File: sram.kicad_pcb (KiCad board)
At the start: 4 copper layers, 25 parts, among them J1 Cache_slot, M1 UM61256AS, M2 UM61256AS, M3 UM61256AS, M4 UM61256AS, M5 UM61256AS, M6 UM61256AS, M7 UM61256AS, M8 UM61256AS, U1 74HCT244, U2 74HCT244

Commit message: 3 errors, 76 warnings
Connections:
- net M1_WE# renamed WE_byte0
- net M8_WE# renamed WE_8
- net Net-(J1-PadA19) renamed under_U1_3
- net Net-(J1-PadA25) renamed under_U1_2
- net U1_2A0 renamed CPU_A8
- net U1_2A1 renamed CPU_A7
- net U1_2A2 renamed CPU_A6
- net U1_2A3 renamed CPU_A5
- net U2_2A0 renamed CPU_A17
- net U2_2A1 renamed CPU_A15
- net U2_2A3 renamed CPU_A16
- net a10 renamed under_tag6
- net a11 renamed under_tag7
- net a13 renamed under_tag8
- net a15 renamed under_tag9
- net a17 renamed under_tag10
- net a18 renamed under_tag11
- net a2 renamed under_tag12
- net a3 renamed under_tag13
- net a35 renamed under_U1_1
- net a4 renamed under_tag14
- net a51 renamed CPU_A13
- net a8 renamed under_tag5
- J1 pad A1: a1 -> unconnected-(J1-PadA1)
- J1 pad A30: a30 -> unconnected-(J1-PadA30)
- J1 pad A31: a31 -> unconnected-(J1-PadA31)
- J1 pad A33: a33 -> unconnected-(J1-PadA33)
- J1 pad A34: a34 -> unconnected-(J1-PadA34)
- J1 pad A42: a42 -> CPU_A9
- J1 pad A43: a43 -> CPU_A10
- J1 pad A45: a45 -> CPU_A11
- J1 pad A46: a46 -> CPU_A12
- J1 pad A49: U2_2A2 -> CPU_A14
- J1 pad A54: a54 -> unconnected-(J1-PadA54)
- J1 pad A55: a55 -> unconnected-(J1-PadA55)
- J1 pad A6: a6 -> unconnected-(J1-PadA6)
- J1 pad A7: a7 -> unconnected-(J1-PadA7)
- J1 pad B15: b15 -> CPU_D31
- J1 pad B16: b16 -> CPU_D30
- J1 pad B17: b17 -> CPU_D29
- J1 pad B19: b19 -> CPU_D28
- J1 pad B20: b20 -> CPU_D27
- J1 pad B21: b21 -> CPU_D26
- J1 pad B23: b23 -> CPU_D25
- J1 pad B24: b24 -> CPU_D24
- J1 pad B25: b25 -> CPU_D23
- J1 pad B27: b27 -> CPU_D22
- J1 pad B28: b28 -> CPU_D21
- J1 pad B29: b29 -> CPU_D20
- J1 pad B31: b31 -> CPU_D19
- J1 pad B32: M3_Q2 -> CPU_D18
- J1 pad B33: M3_Q1 -> CPU_D17
- J1 pad B35: M3_Q0 -> CPU_D16
- J1 pad B36: M6_Q7 -> CPU_D15
- J1 pad B37: M6_Q6 -> CPU_D14
- J1 pad B39: b39 -> CPU_D13
- J1 pad B40: b40 -> CPU_D12
- J1 pad B41: b41 -> CPU_D11
- J1 pad B43: M6_Q2 -> CPU_D10
- J1 pad B44: M6_Q1 -> CPU_D9
- J1 pad B45: M6_Q0 -> CPU_D8
- J1 pad B47: M5_Q7 -> CPU_D7
- J1 pad B48: M5_Q6 -> CPU_D6
- J1 pad B49: M5_Q5 -> CPU_D5
- J1 pad B51: M5_Q4 -> CPU_D4
- J1 pad B52: M5_Q3 -> CPU_D3
- J1 pad B53: M5_Q2 -> CPU_D2
- J1 pad B55: M5_Q1 -> CPU_D1
- J1 pad B56: M5_Q0 -> CPU_D0
- M1 pad 11: M1_Q0 -> CPU_D0
- M1 pad 12: M1_Q1 -> CPU_D1
- M1 pad 13: M1_Q2 -> CPU_D2
- M1 pad 15: M1_Q3 -> CPU_D3
- M1 pad 16: M1_Q4 -> CPU_D4
- M1 pad 17: M1_Q5 -> CPU_D5
- M1 pad 18: M1_Q6 -> CPU_D6
- M1 pad 19: M1_Q7 -> CPU_D7
- M1 pad 20: unconnected-(M1-~{CS}-Pad20) -> Bank0_CS
- M1 pad 22: unconnected-(M1-~{OE}-Pad22) -> Bank0_OE
- M2 pad 11: M2_Q0 -> CPU_D8
- M2 pad 12: M2_Q1 -> CPU_D9
- M2 pad 13: M2_Q2 -> CPU_D10
- M2 pad 15: M2_Q3 -> CPU_D11
- M2 pad 16: M2_Q4 -> CPU_D12
- M2 pad 17: M2_Q5 -> CPU_D13
- M2 pad 18: M2_Q6 -> CPU_D14
- M2 pad 19: M2_Q7 -> CPU_D15
- M2 pad 20: unconnected-(M2-~{CS}-Pad20) -> Bank0_CS
- M2 pad 22: unconnected-(M2-~{OE}-Pad22) -> Bank0_OE
- M3 pad 11: M3_Q0 -> CPU_D16
- M3 pad 12: M3_Q1 -> CPU_D17
- M3 pad 13: M3_Q2 -> CPU_D18
- M3 pad 15: M3_Q3 -> CPU_D19
- M3 pad 16: M3_Q4 -> CPU_D20
- M3 pad 17: M3_Q5 -> CPU_D21
- M3 pad 18: M3_Q6 -> CPU_D22
- M3 pad 19: M3_Q7 -> CPU_D23
- M3 pad 20: unconnected-(M3-~{CS}-Pad20) -> Bank0_CS
- M3 pad 22: unconnected-(M3-~{OE}-Pad22) -> Bank0_OE
- M4 pad 11: M4_Q0 -> CPU_D24
- M4 pad 12: M4_Q1 -> CPU_D25
- M4 pad 13: M4_Q2 -> CPU_D26
- M4 pad 15: M4_Q3 -> CPU_D27
- M4 pad 16: M4_Q4 -> CPU_D28
- M4 pad 17: M4_Q5 -> CPU_D29
- M4 pad 18: M4_Q6 -> CPU_D30
- M4 pad 19: M4_Q7 -> CPU_D31
- M4 pad 20: unconnected-(M4-~{CS}-Pad20) -> Bank0_CS
- M4 pad 22: unconnected-(M4-~{OE}-Pad22) -> Bank0_OE
- M5 pad 11: M5_Q0 -> CPU_D0
- M5 pad 12: M5_Q1 -> CPU_D1
- M5 pad 13: M5_Q2 -> CPU_D2
- M5 pad 15: M5_Q3 -> CPU_D3
- M5 pad 16: M5_Q4 -> CPU_D4
- M5 pad 17: M5_Q5 -> CPU_D5
- M5 pad 18: M5_Q6 -> CPU_D6
- M5 pad 19: M5_Q7 -> CPU_D7
- M5 pad 20: unconnected-(M5-~{CS}-Pad20) -> Bank1_CS
- M5 pad 22: unconnected-(M5-~{OE}-Pad22) -> Bank1_OE
- M6 pad 11: M6_Q0 -> CPU_D8
- M6 pad 12: M6_Q1 -> CPU_D9
- M6 pad 13: M6_Q2 -> CPU_D10
- M6 pad 15: M6_Q3 -> CPU_D11
- M6 pad 16: M6_Q4 -> CPU_D12
- M6 pad 17: M6_Q5 -> CPU_D13
- M6 pad 18: M6_Q6 -> CPU_D14
- M6 pad 19: M6_Q7 -> CPU_D15
- M6 pad 20: unconnected-(M6-~{CS}-Pad20) -> Bank1_CS
- M6 pad 22: unconnected-(M6-~{OE}-Pad22) -> Bank1_OE
- M7 pad 11: M7_Q0 -> CPU_D16
- M7 pad 12: M7_Q1 -> CPU_D17
- M7 pad 13: M7_Q2 -> CPU_D18
- M7 pad 15: M7_Q3 -> CPU_D19
- M7 pad 16: M7_Q4 -> CPU_D20
- M7 pad 17: M7_Q5 -> CPU_D21
- M7 pad 18: M7_Q6 -> CPU_D22
- M7 pad 19: M7_Q7 -> CPU_D23
- M7 pad 20: unconnected-(M7-~{CS}-Pad20) -> Bank1_CS
- M7 pad 22: unconnected-(M7-~{OE}-Pad22) -> Bank1_OE
- M7 pad 27: unconnected-(M7-~{WE}-Pad27) -> WE_7
- M8 pad 11: M8_Q0 -> CPU_D24
- M8 pad 12: M8_Q1 -> CPU_D25
- M8 pad 13: M8_Q2 -> CPU_D26
- M8 pad 15: M8_Q3 -> CPU_D27
- M8 pad 16: M8_Q4 -> CPU_D28
- M8 pad 17: M8_Q5 -> CPU_D29
- M8 pad 18: M8_Q6 -> CPU_D30
- M8 pad 19: M8_Q7 -> CPU_D31
- M8 pad 20: unconnected-(M8-~{CS}-Pad20) -> Bank1_CS
- M8 pad 22: unconnected-(M8-~{OE}-Pad22) -> Bank1_OE
- MD1 pad 21: MD1_A10 -> CPU_A14
- MD1 pad 24: MD1_A9 -> CPU_A12
- MD1 pad 25: MD1_A8 -> CPU_A11
- R6 pad 1: unconnected-(R6-Pad1) -> under_tag3
- U1 pad 6: unconnected-(U1-1A2-Pad6) -> under_tag4
- U2 pad 12: unconnected-(U2-1Y3-Pad12) -> CPU_A4_SR
- U2 pad 13: U2_2A2 -> CPU_A14
- U2 pad 2: unconnected-(U2-1A0-Pad2) -> CPU_A12
- U2 pad 4: MD1_A8 -> CPU_A11
- U2 pad 6: unconnected-(U2-1A2-Pad6) -> CPU_A10
- U2 pad 8: unconnected-(U2-1A3-Pad8) -> CPU_A9
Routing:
- net Bank1_OE: track 0.00 -> 163.9 mm, vias 0 -> 8
- net (no net): track 312.1 -> 155.4 mm, vias 32 -> 8
- net Bank0_OE: track 0.00 -> 151.3 mm, vias 0 -> 4
- net Bank0_CS: track 0.00 -> 120.9 mm, vias 0 -> 3
- net Bank1_CS: track 0.00 -> 113.4 mm, vias 0 -> 2
- net unconnected-(M4-~{CS}-Pad20): track 92.0 -> 0.00 mm, vias 3 -> 0
- net unconnected-(M1-~{OE}-Pad22): track 88.8 -> 0.00 mm, vias 2 -> 0
- net unconnected-(M5-~{OE}-Pad22): track 86.5 -> 0.00 mm, vias 3 -> 0
- net unconnected-(M5-~{CS}-Pad20): track 81.9 -> 0.00 mm, vias 2 -> 0
- net CPU_A14: track 0.00 -> 56.9 mm, vias 0 -> 2
- net CPU_A12: track 0.00 -> 55.1 mm, vias 0 -> 2
- net CPU_A11: track 0.00 -> 52.2 mm, vias 0 -> 2
- net CPU_A9: track 0.00 -> 51.6 mm
- net CPU_A4_SR: track 78.8 -> 128.9 mm, vias 4 -> 6
- net CPU_A10: track 0.00 -> 48.7 mm
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
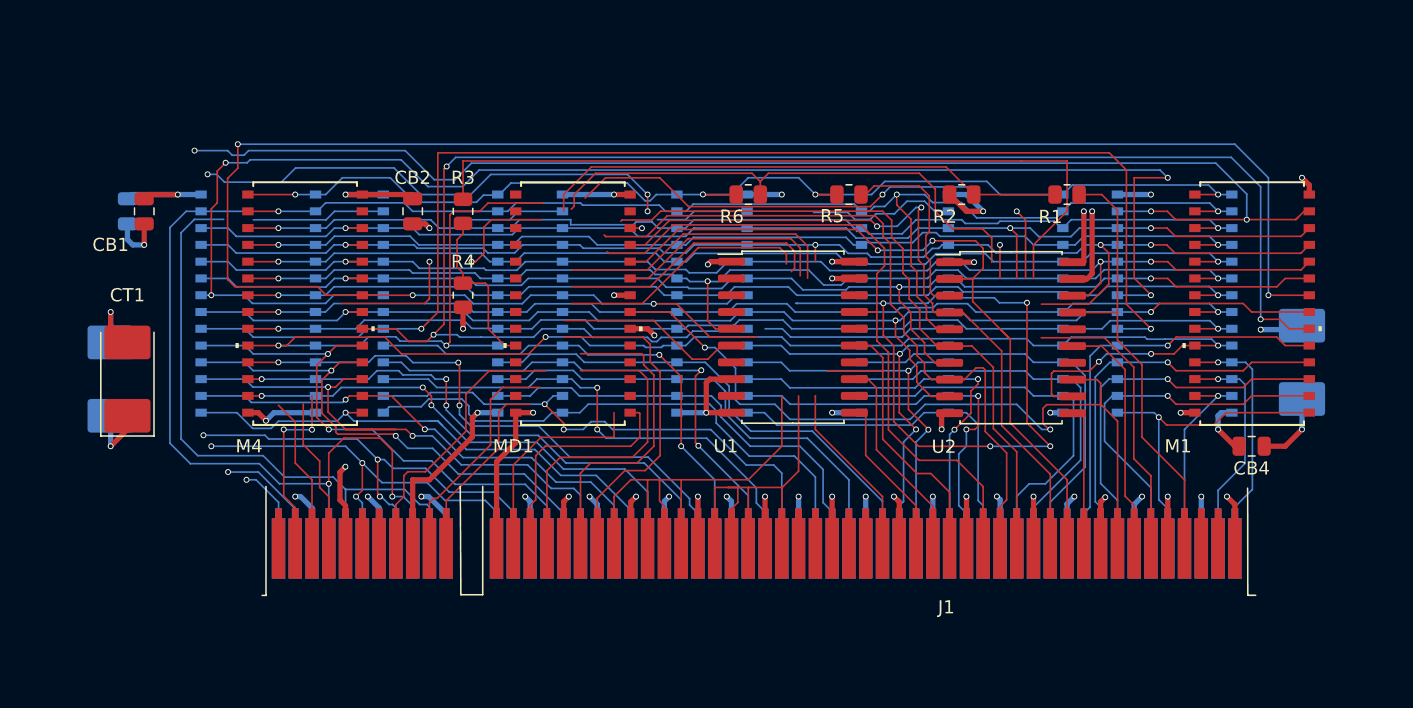
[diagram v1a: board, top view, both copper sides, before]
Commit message: 0 drc errors, 62 violations
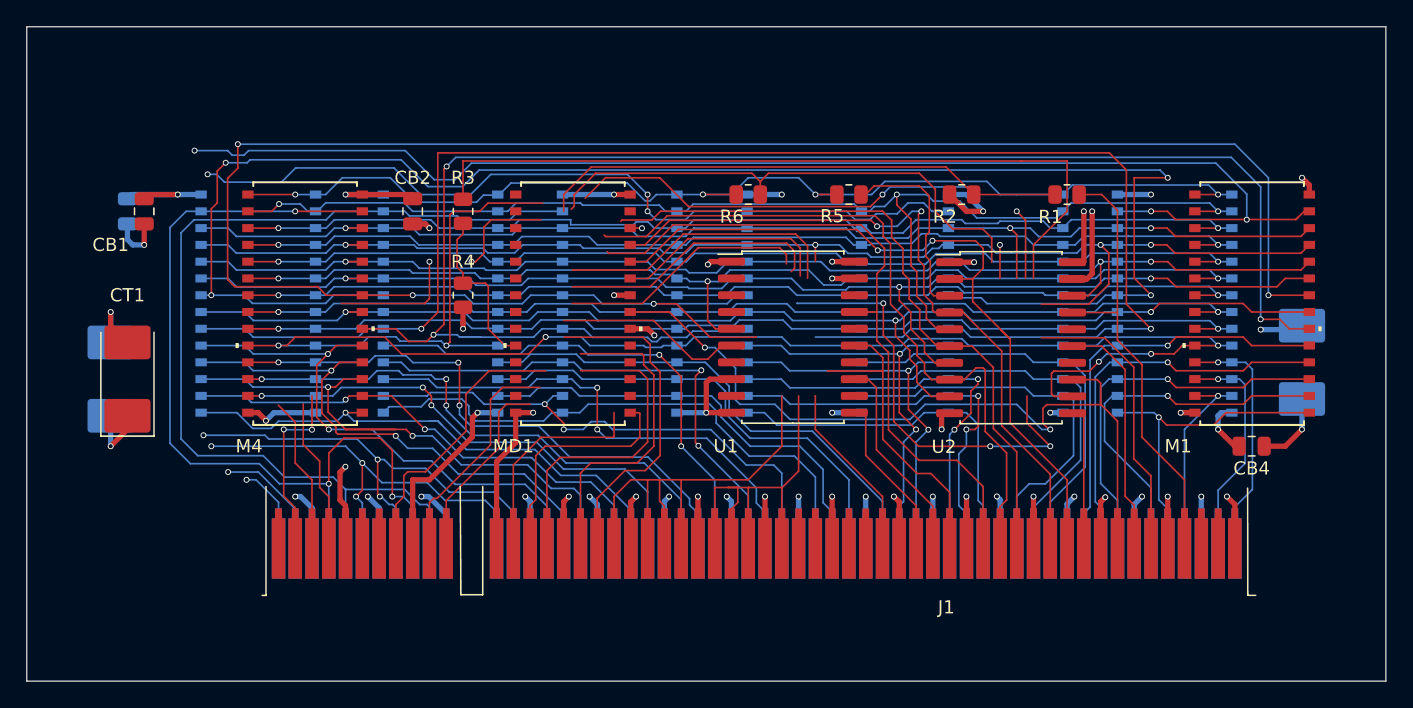
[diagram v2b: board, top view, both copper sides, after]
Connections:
- net ?1 renamed under_sticker1
- net ?2 renamed under_sticker2
- net ?3 renamed under_sticker3
- net ?4 renamed under_sticker4
- J1 pad B10: ?7 -> WE_byte2
- J1 pad B4: WE_8 -> WE_byte3
- J1 pad B5: ?7 -> WE_byte2
- J1 pad B9: WE_8 -> WE_byte3
- M2 pad 27: unconnected-(M2-~{WE}-Pad27) -> WE_byte1
- M3 pad 27: unconnected-(M3-~{WE}-Pad27) -> WE_byte2
- M4 pad 27: unconnected-(M4-~{WE}-Pad27) -> WE_byte3
- M6 pad 27: unconnected-(M6-~{WE}-Pad27) -> WE_byte1
- M7 pad 27: WE_7 -> WE_byte2
- M8 pad 27: WE_8 -> WE_byte3
- R3 pad 2: unconnected-(R3-Pad2) -> under_U2_4
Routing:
- net WE_byte2: track 0.00 -> 69.0 mm
- net WE_byte1: track 0.00 -> 61.7 mm, vias 0 -> 3
- net WE_byte3: track 0.00 -> 60.8 mm, vias 0 -> 3
- net under_U2_4: track 0.00 -> 58.6 mm
- net unconnected-(R3-Pad2): track 58.6 -> 0.00 mm
- net WE_8: track 51.9 -> 0.00 mm, vias 2 -> 0
- net ?7: track 42.5 -> 0.00 mm
- net Bank1_OE: track 163.9 -> 125.6 mm, vias 8 -> 4
- net unconnected-(M6-~{WE}-Pad27): track 11.3 -> 0.00 mm
- net WE_7: track 10.1 -> 0.00 mm
- net Bank1_CS: track 113.4 -> 122.7 mm
- net unconnected-(M3-~{WE}-Pad27): track 7.92 -> 0.00 mm
- net unconnected-(M2-~{WE}-Pad27): track 7.04 -> 0.00 mm
- net (no net): track 155.4 -> 150.9 mm
- net Bank0_CS: track 120.9 -> 122.5 mm
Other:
- board outline added: 102.9 x 49.5 mm

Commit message: 90% there, 0 errors 18 warnings. Just a couple tracks left.
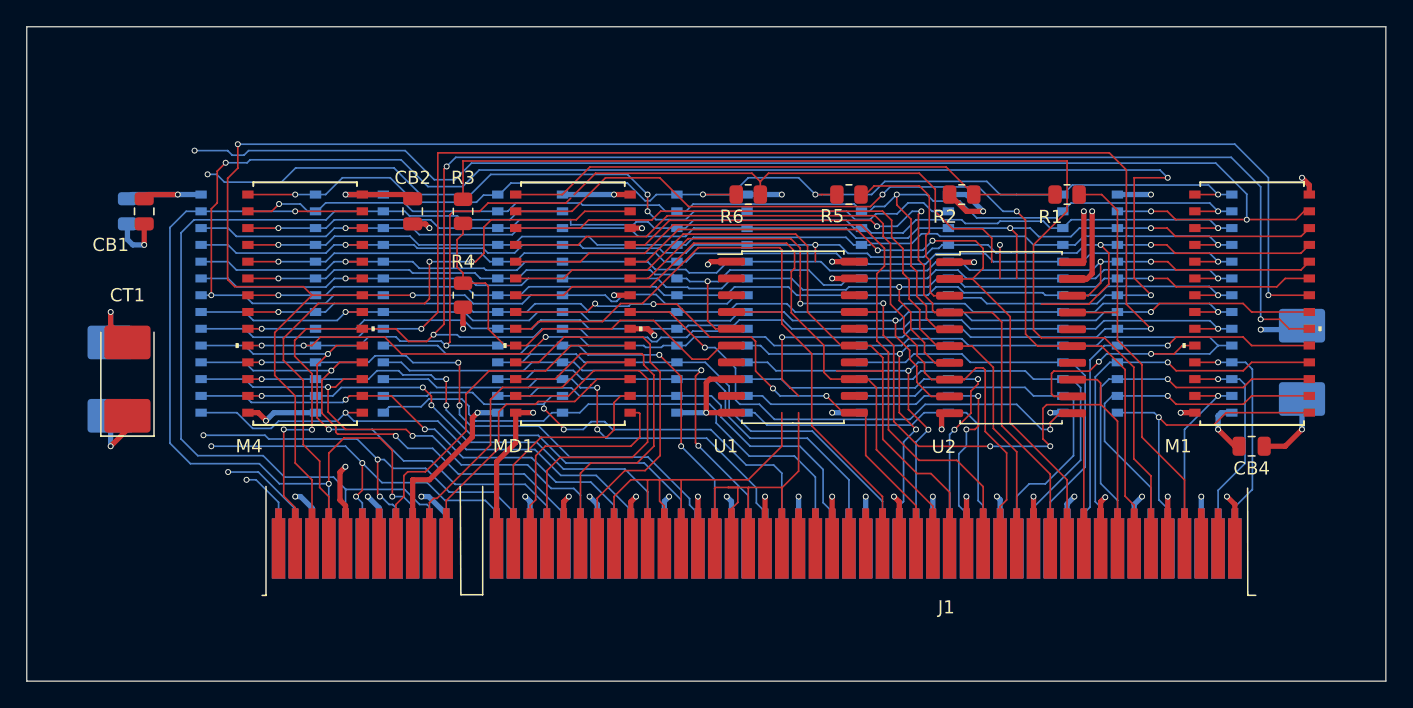
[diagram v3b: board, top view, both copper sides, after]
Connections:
- net WE_byte0 renamed Byte_WE0
- net WE_byte1 renamed Byte_WE1
- net WE_byte2 renamed Byte_WE2
- net WE_byte3 renamed Byte_WE3
- J1 pad A10: under_tag6 -> TAG_Q6
- J1 pad A11: under_tag7 -> TAG_Q5
- J1 pad A13: under_tag8 -> TAG_Q4
- J1 pad A15: under_tag9 -> TAG_Q2
- J1 pad A17: under_tag10 -> TAG_Q1
- J1 pad A18: under_tag11 -> TAG_Q0
- J1 pad A2: under_tag12 -> Bank0_CS
- J1 pad A3: under_tag13 -> Bank0_OE
- J1 pad A4: under_tag14 -> TAG_WE
- J1 pad A8: under_tag5 -> TAG_Q7
- J1 pad B14: GND -> +5V
- J1 pad B18: GND -> +5V
- J1 pad B26: GND -> +5V
- J1 pad B38: GND -> +5V
- J1 pad B42: GND -> +5V
- J1 pad B46: GND -> +5V
- J1 pad B50: GND -> +5V
- J1 pad B7: GND -> +5V
- MD1 pad 1: MD1_A14 -> TAG_A14
- MD1 pad 10: MD1_A0 -> TAG_A0
- MD1 pad 2: MD1_A12 -> CPU_A15
- MD1 pad 21: CPU_A14 -> CPU_A16
- MD1 pad 23: MD1_A11 -> CPU_A14
- MD1 pad 26: MD1_A13 -> +5V
- MD1 pad 27: unconnected-(MD1-~{WE}-Pad27) -> TAG_WE
- MD1 pad 3: MD1_A7 -> CPU_A10
- MD1 pad 4: MD1_A6 -> CPU_A9
- MD1 pad 5: MD1_A5 -> CPU_A8
- MD1 pad 6: MD1_A4 -> CPU_A7
- MD1 pad 7: MD1_A3 -> CPU_A6
- MD1 pad 8: MD1_A2 -> CPU_A5
- MD1 pad 9: MD1_A1 -> under_U1_1
- R1 pad 1: Net-(R1-Pad1) -> TAG_A14
- R2 pad 2: Net-(R1-Pad1) -> TAG_A14
- R3 pad 1: MD1_A0 -> TAG_A0
- R3 pad 2: under_U2_4 -> CPU_A13
- R4 pad 1: MD1_A0 -> TAG_A0
- R4 pad 2: GND -> +5V
- U1 pad 4: unconnected-(U1-1A1-Pad4) -> under_U1_1
- U1 pad 6: under_tag4 -> TAG_A0
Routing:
- net (no net): track 150.9 -> 2.54 mm, vias 8 -> 1
- net CPU_A13: track 19.5 -> 82.8 mm
- net under_U2_4: track 58.6 -> 0.00 mm
- net CPU_A15: track 15.9 -> 70.6 mm, vias 0 -> 2
- net TAG_WE: track 0.00 -> 47.7 mm, vias 0 -> 2
- net TAG_A14: track 0.00 -> 42.5 mm
- net CPU_A16: track 8.26 -> 48.7 mm, vias 0 -> 2
- net Net-(R1-Pad1): track 40.2 -> 0.00 mm
- net under_U1_1: track 11.0 -> 49.7 mm
- net CPU_A6: track 13.2 -> 49.0 mm
- net CPU_A7: track 21.2 -> 54.0 mm
- net TAG_A0: track 0.00 -> 31.5 mm
- net CPU_A5: track 10.1 -> 41.0 mm, vias 0 -> 4
- net TAG_Q2: track 0.00 -> 27.6 mm
- net TAG_Q0: track 0.00 -> 27.2 mm
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
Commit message: 95% there, 0 errors, 7 Warnings. 5 connections missing, 11 guesses and assumptions on U1 U2 and some more on common lines.
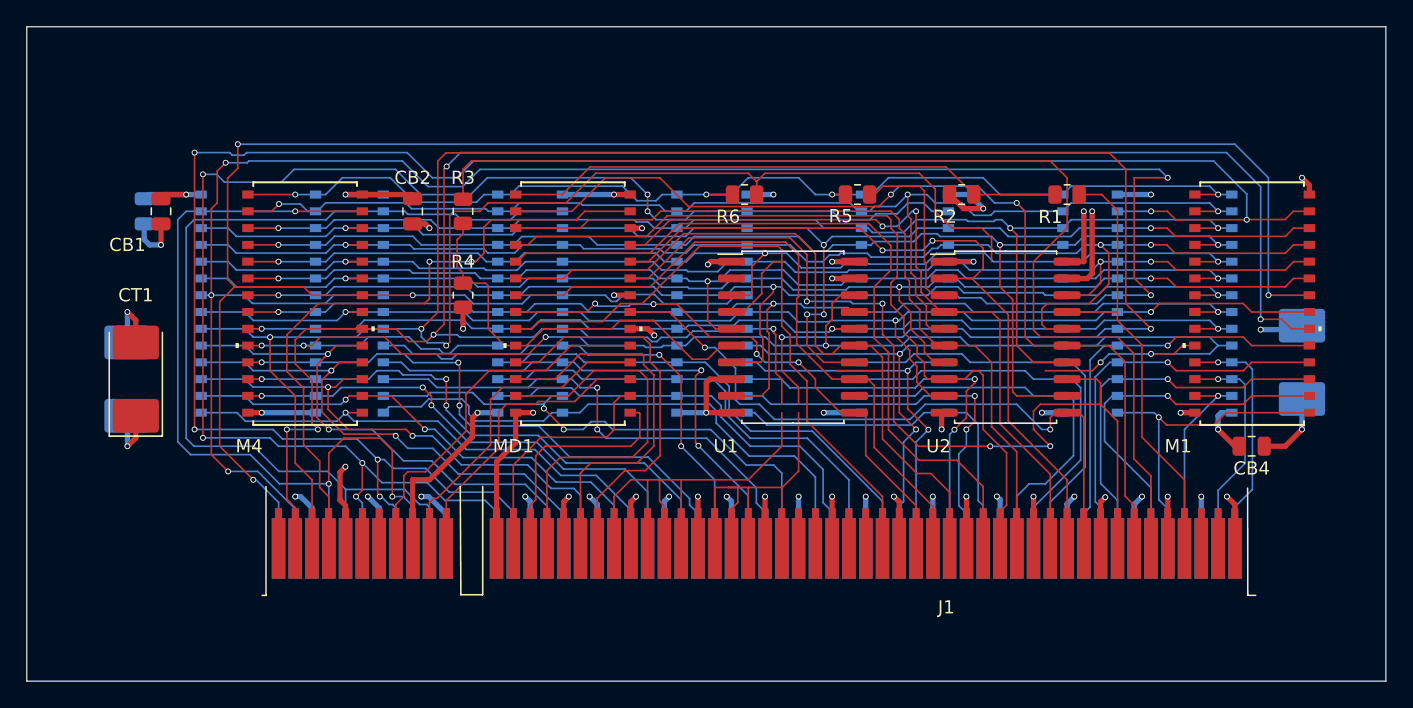
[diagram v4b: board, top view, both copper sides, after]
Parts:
- moved CB1 1.27 mm to (125.7, 83.8)
- moved CB3 1.27 mm to (124.5, 83.8)
- moved CT2 1.27 mm to (123.2, 96.5)
- moved R5 0.65 mm to (178.4, 82.5)
- moved CT1 0.64 mm to (123.8, 96.5)
- moved U2 0.41 mm to (189.7, 93.3)
- moved R6 0.28 mm to (169.9, 82.5)
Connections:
- net under_U1_1 renamed CPU_A4
- J1 pad A3: Bank0_OE -> Bank1_CS
- J1 pad A47: CPU_A16 -> CPU_A13
- J1 pad A51: CPU_A13 -> CPU_A16
- J1 pad B1: under_sticker3 -> Bank0_OE
- J1 pad B12: under_sticker1 -> Byte_WE1
- J1 pad B13: under_sticker2 -> Byte_WE0
- J1 pad B2: under_sticker4 -> Bank1_OE
- J1 pad B6: under_sticker1 -> Byte_WE1
- J1 pad B8: under_sticker2 -> Byte_WE0
- MD1 pad 21: CPU_A16 -> CPU_A13
- R3 pad 2: CPU_A13 -> CPU_A16
- R6 pad 1: under_tag3 -> Bank1_CS
- U1 pad 14: unconnected-(U1-1Y2-Pad14) -> CPU_A17_SR
- U1 pad 16: unconnected-(U1-1Y1-Pad16) -> CPU_A5_SR
- U1 pad 18: unconnected-(U1-1Y0-Pad18) -> CPU_A4_SR
- U1 pad 3: unconnected-(U1-2Y0-Pad3) -> CPU_A9_SR
- U1 pad 7: unconnected-(U1-2Y2-Pad7) -> CPU_A7_SR
- U1 pad 9: unconnected-(U1-2Y3-Pad9) -> CPU_A6_SR
- U2 pad 11: CPU_A16 -> CPU_A13
- U2 pad 12: CPU_A4_SR -> CPU_A10_SR
- U2 pad 14: unconnected-(U2-1Y2-Pad14) -> CPU_A11_SR
- U2 pad 16: unconnected-(U2-1Y1-Pad16) -> CPU_A12_SR
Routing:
- net Bank1_CS: track 130.1 -> 206.5 mm, vias 3 -> 5
- net Byte_WE0: track 99.3 -> 151.8 mm, vias 3 -> 6
- net Byte_WE1: track 61.7 -> 110.6 mm, vias 3 -> 6
- net under_tag3: track 38.6 -> 0.00 mm
- net CPU_A13: track 82.8 -> 48.9 mm, vias 0 -> 2
- net CPU_A16: track 48.7 -> 82.3 mm, vias 2 -> 0
- net under_sticker2: track 30.8 -> 0.00 mm, vias 3 -> 0
- net under_sticker1: track 28.0 -> 0.00 mm, vias 3 -> 0
- net Bank1_OE: track 125.6 -> 146.0 mm, vias 4 -> 5
- net CPU_A4_SR: track 132.9 -> 116.3 mm
- net CPU_A10_SR: track 79.0 -> 95.2 mm, vias 2 -> 3
- net CPU_A11_SR: track 79.7 -> 92.7 mm, vias 2 -> 3
- net CPU_A6_SR: track 78.8 -> 88.6 mm, vias 2 -> 3
- net CPU_A17_SR: track 92.3 -> 101.7 mm, vias 3 -> 5
- net Bank0_CS: track 142.5 -> 151.1 mm, vias 5 -> 6
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
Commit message: 99% done, ERC DRC 0 errors 0 warnings
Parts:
- CB1, CB2, CB3, CB4: value C -> 1uF 16V
- CT1, CT2, CT3: value C_Polarized -> 10uF 16V
- J1: footprint UM61256AS:Cache slot -> footprints:Cache slot
- M1, M2, M3, M4, M5, M6, M7, M8, MD1: footprint UM61256AS:SOJ28_18P54X7P75_ISI -> footprints:SOJ28_18P54X7P75_ISI
- U1, U2: value 74HCT244 -> 74F244
- moved J1 2.26 mm to (171.4, 109.2), turned to 0 degrees
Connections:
- M1 pad 10: CPU_A4_SR -> Bank0_A0
- M2 pad 10: CPU_A4_SR -> Bank0_A0
- M3 pad 10: CPU_A4_SR -> Bank0_A0
- M4 pad 10: CPU_A4_SR -> Bank0_A0
- M5 pad 10: CPU_A4_SR -> Bank1_A0
- M6 pad 10: CPU_A4_SR -> Bank1_A0
- M7 pad 10: CPU_A4_SR -> Bank1_A0
- M8 pad 10: CPU_A4_SR -> Bank1_A0
- R6 pad 1: Bank1_CS -> Bank1_A0
- U1 pad 18: CPU_A4_SR -> unconnected-(U1-1Y0-Pad18)
- U1 pad 2: unconnected-(U1-1A0-Pad2) -> GND
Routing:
- net Bank1_A0: track 0.00 -> 116.4 mm, vias 0 -> 3
- net CPU_A4_SR: track 116.3 -> 0.00 mm, vias 6 -> 0
- net Bank0_A0: track 0.00 -> 97.7 mm, vias 0 -> 6
- net GND: track 104.7 -> 154.5 mm
- net Bank1_CS: track 206.5 -> 160.2 mm, vias 5 -> 3
- net under_U1_3: track 25.9 -> 0.00 mm
- net under_U1_2: track 20.1 -> 0.00 mm
- net +5V: track 64.5 -> 82.7 mm
- net Bank0_CS: track 151.1 -> 166.2 mm, vias 6 -> 4
- net Byte_WE3: track 59.9 -> 65.3 mm
- net Byte_WE1: track 110.6 -> 115.7 mm
- net Byte_WE0: track 151.8 -> 156.7 mm
- net Byte_WE2: track 68.3 -> 73.1 mm
- net CPU_D24: track 41.9 -> 45.0 mm
- net CPU_A5: track 40.5 -> 43.4 mm
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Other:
- board size 102.9 x 49.5 mm -> 97.8 x 28.2 mm

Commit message: are we done?
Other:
- board size 97.8 x 28.2 mm -> 97.2 x 28.2 mm
- board text added: "2.2"
- board text added: "256KB of Majestic L2 Cache for FIC 486-GAC-2"
- board text added: "Bank 0"
- board text added: "Bank 1"
- board text added: "Config: 256K (bank 0,1) R1 R3 R5 | 128K (bank 0) R2 R3 R6 | 64KB (bank 0,1) R2 R4"
- board text added: "JLCJLCJLCJLC"
- board text added: "MODEL: CACHE MODULE DOC: 13630"
- board text added: "Reverse engineered in Poland"
- board text added: "Tag"
- board text added: "by Rasz_pl"
